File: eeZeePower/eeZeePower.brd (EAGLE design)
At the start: 26 x 12.7 mm, 11 parts

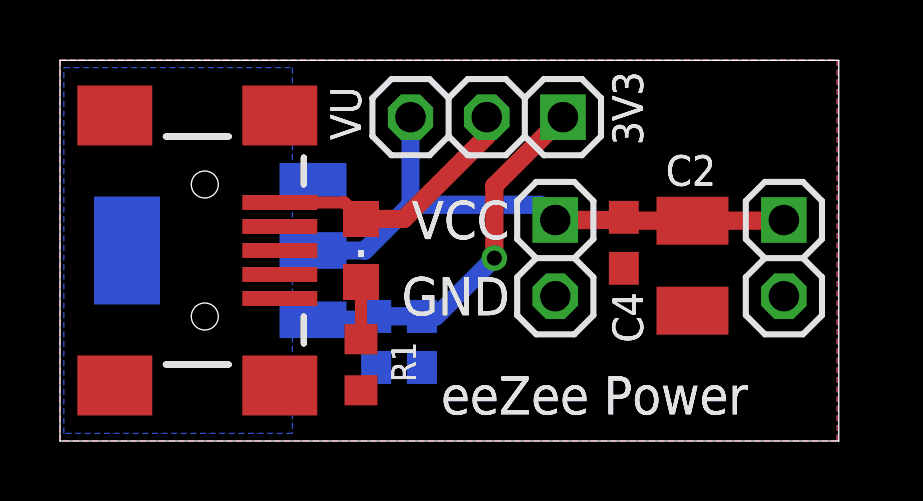
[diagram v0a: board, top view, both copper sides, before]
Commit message: Rev 0.3 converted to standard 1206 LED, centered components, mitered corners, moved some components around, removed component names.
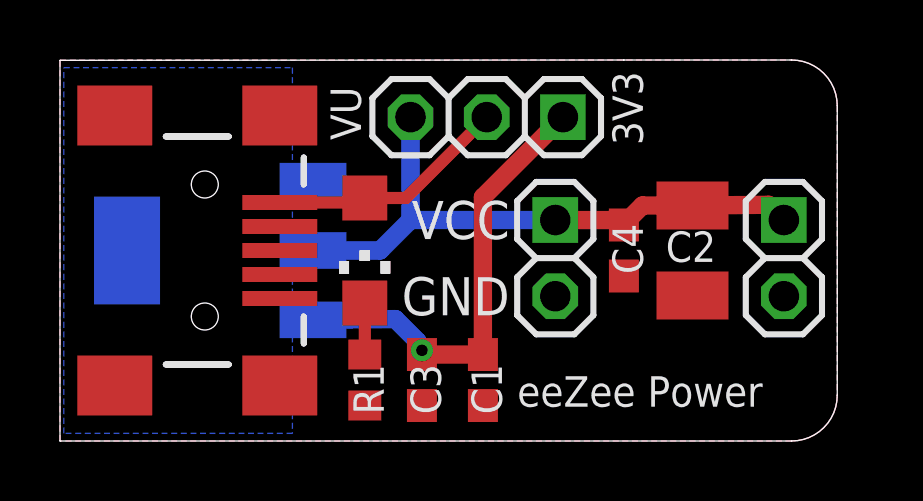
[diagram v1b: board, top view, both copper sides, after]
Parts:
- LED1: device led:CHIPLED_0805 -> led:CHIPLED_1206
- moved C1 2.40 mm to (14.1, 2.03), flipped to the top
- moved C3 1.98 mm to (12.1, 2.03), flipped to the top
- moved R1 0.52 mm to (10.2, 2.03)
- moved C2 0.51 mm to (21.1, 6.35)
- moved C4 0.25 mm to (18.8, 6.35)
- moved LED1 0.13 mm to (10.2, 6.35)
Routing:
- net VIN: track 12.5 -> 15.3 mm
- net VBUS: track 8.90 -> 8.03 mm
- net VOUT: track 19.6 -> 20.2 mm
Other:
- board size 26 x 12.7 mm -> 25.9 x 12.7 mm
- board text added: "Rev 0.3"
- board text removed: "C1"
- board text removed: "C2"
- board text removed: "C3"
- board text removed: "C4"
- board text removed: "R1"
- board text removed: "Rev 0.1"
- board text removed: "Rev 0.2"
- board text removed: "U1"

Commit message: Converted to standard 1206 10uF, placed input bypass caps on bottom. Rearranged silk, centered pin headers.
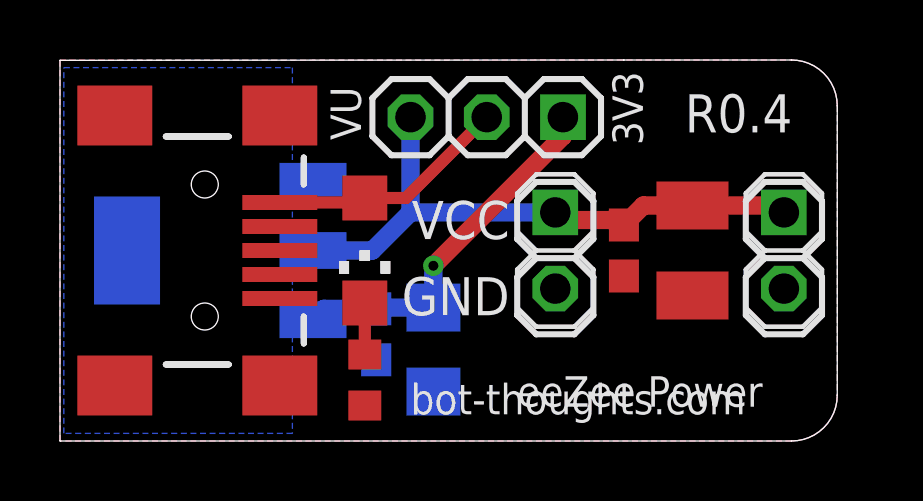
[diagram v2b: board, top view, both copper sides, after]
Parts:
- C3: device rcl:C0603 -> rcl:C1206
- moved C1 3.87 mm to (10.5, 3.56), flipped to the bottom
- moved C3 1.09 mm to (12.4, 3.05), flipped to the bottom
- moved JP3 0.25 mm to (16.5, 6.35)
- moved JP4 0.25 mm to (24.1, 6.35)
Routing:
- net VIN: track 15.3 -> 12.3 mm
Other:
- board text added: "R0.4"
